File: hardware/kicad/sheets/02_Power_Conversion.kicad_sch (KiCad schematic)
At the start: 77 parts, among them U201 LMR38020F-Q1 adjustable-frequ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, U202 TPS2121RUXR priority power mux, U203 4.4..5.25 V synchronous buck 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, U204 SN74LVC1G08-Q1 — MAIN_INPUT_V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, U205 SN74LVC08A-Q1 quad AND — requ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, U206 TPS22918-Q1 OLED load switch, U207 TPS22918-Q1 SENSOR load switch, U208 TPS22918-Q1 UI load switch, U209 TPS2553-Q1 active-high EXPANS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, U210 TPS22918-Q1 RELAY logic branch, U211 TPS22918-Q1 FIELD-SENSE branch, U212 TPS2553-Q1 active-high motor-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, U213 TPS2553-Q1 active-high motor-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

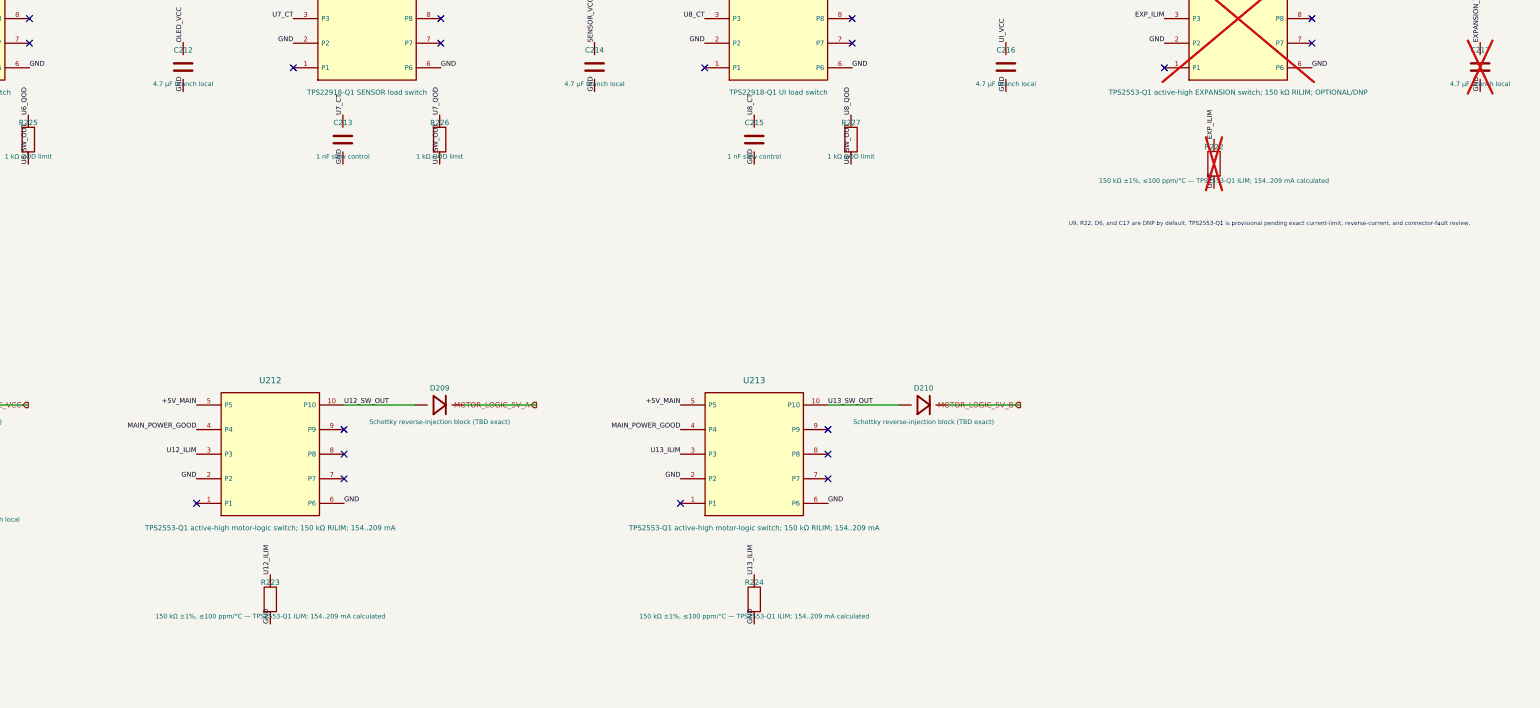
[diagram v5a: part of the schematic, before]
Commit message: Implement ECO-008R TPS2553 current limits
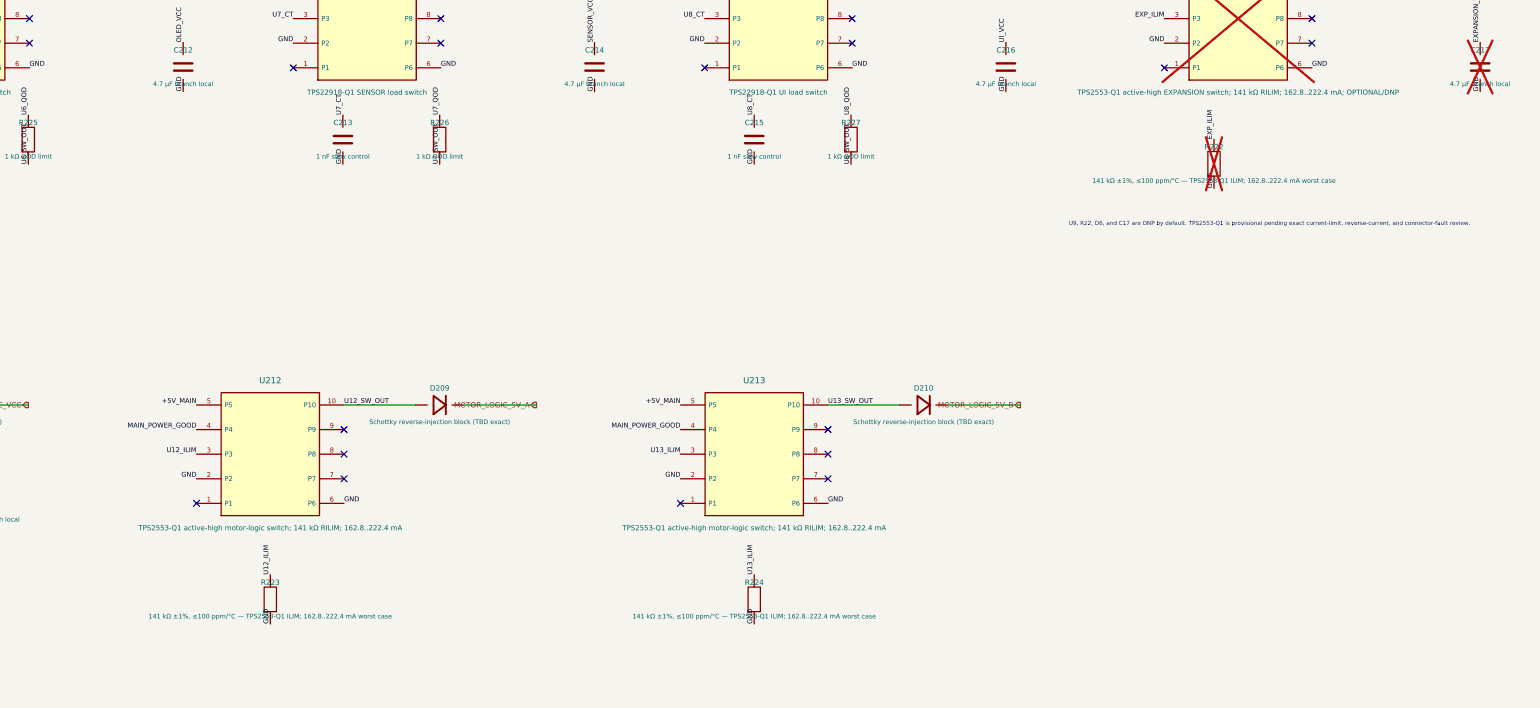
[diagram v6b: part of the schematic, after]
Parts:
- R222, R223, R224: value 150 kΩ ±1%, ≤100 ppm/°C — TPS2553-Q1 ILIM; 154..209 mA calculated -> 141 kΩ ±1%, ≤100 ppm/°C — TPS2553-Q1 ILIM; 162.8..222.4 mA worst case
- U209: value TPS2553-Q1 active-high EXPANSION switch; 150 kΩ RILIM; OPTIONAL/DNP -> TPS2553-Q1 active-high EXPANSION switch; 141 kΩ RILIM; 162.8..222.4 mA; OPTIONAL/DNP
- U212, U213: value TPS2553-Q1 active-high motor-logic switch; 150 kΩ RILIM; 154..209 mA -> TPS2553-Q1 active-high motor-logic switch; 141 kΩ RILIM; 162.8..222.4 mA
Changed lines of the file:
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@@
   (symbol (lib_id "IPC100:IC10") (at 455 155 0) (unit 1) (exclude_from_sim no) (in_bom yes) (on_board yes) (dnp yes)
     (property "Reference" "U209" (at 455 139.76 0) (effects (font (size 1.27 1.27))))
-    (property "Value" "TPS2553-Q1 active-high EXPANSION switch; 150 kΩ RILIM; OPTIONAL/DNP" (at 455 170.24 0) (effects (font (size 1.05 1.05))))
+    (property "Value" "TPS2553-Q1 active-high EXPANSION switch; 141 kΩ RILIM; 162.8..222.4 mA; OPTIONAL/DNP" (at 455 170.24 0) (effects (font (size 1.05 1.05))))
     (property "Footprint" "" (at 455 155 0) (effects (font (size 1 1)) hide))
     (property "Datasheet" "https://www.ti.com/lit/ds/symlink/tps2553-q1.pdf" (at 455 155 0) (effects (font (size 1 1)) hide))
@@
   (symbol (lib_id "IPC100:R") (at 450 185 90) (unit 1) (exclude_from_sim no) (in_bom yes) (on_board yes) (dnp yes)
     (property "Reference" "R222" (at 450 181.5 90) (effects (font (size 1.1 1.1))))
-    (property "Value" "150 kΩ ±1%, ≤100 ppm/°C — TPS2553-Q1 ILIM; 154..209 mA calculated" (at 450 188.5 90) (effects (font (size 0.95 0.95))))
+    (property "Value" "141 kΩ ±1%, ≤100 ppm/°C — TPS2553-Q1 ILIM; 162.8..222.4 mA worst case" (at 450 188.5 90) (effects (font (size 0.95 0.95))))
     (property "Footprint" "" (at 450 185 0) (effects (font (size 1 1)) hide))
     (property "Datasheet" "" (at 450 185 0) (effects (font (size 1 1)) hide))
@@
   (symbol (lib_id "IPC100:IC10") (at 255 245 0) (unit 1) (exclude_from_sim no) (in_bom yes) (on_board yes) (dnp no)
     (property "Reference" "U212" (at 255 229.76 0) (effects (font (size 1.27 1.27))))
-    (property "Value" "TPS2553-Q1 active-high motor-logic switch; 150 kΩ RILIM; 154..209 mA" (at 255 260.24 0) (effects (font (size 1.05 1.05))))
+    (property "Value" "TPS2553-Q1 active-high motor-logic switch; 141 kΩ RILIM; 162.8..222.4 mA" (at 255 260.24 0) (effects (font (size 1.05 1.05))))
     (property "Footprint" "" (at 255 245 0) (effects (font (size 1 1)) hide))
     (property "Datasheet" "https://www.ti.com/lit/ds/symlink/tps2553-q1.pdf" (at 255 245 0) (effects (font (size 1 1)) hide))
@@
   (symbol (lib_id "IPC100:R") (at 255 275 90) (unit 1) (exclude_from_sim no) (in_bom yes) (on_board yes) (dnp no)
     (property "Reference" "R223" (at 255 271.5 90) (effects (font (size 1.1 1.1))))
-    (property "Value" "150 kΩ ±1%, ≤100 ppm/°C — TPS2553-Q1 ILIM; 154..209 mA calculated" (at 255 278.5 90) (effects (font (size 0.95 0.95))))
+    (property "Value" "141 kΩ ±1%, ≤100 ppm/°C — TPS2553-Q1 ILIM; 162.8..222.4 mA worst case" (at 255 278.5 90) (effects (font (size 0.95 0.95))))
     (property "Footprint" "" (at 255 275 0) (effects (font (size 1 1)) hide))
     (property "Datasheet" "" (at 255 275 0) (effects (font (size 1 1)) hide))
@@
   (symbol (lib_id "IPC100:IC10") (at 355 245 0) (unit 1) (exclude_from_sim no) (in_bom yes) (on_board yes) (dnp no)
     (property "Reference" "U213" (at 355 229.76 0) (effects (font (size 1.27 1.27))))
-    (property "Value" "TPS2553-Q1 active-high motor-logic switch; 150 kΩ RILIM; 154..209 mA" (at 355 260.24 0) (effects (font (size 1.05 1.05))))
+    (property "Value" "TPS2553-Q1 active-high motor-logic switch; 141 kΩ RILIM; 162.8..222.4 mA" (at 355 260.24 0) (effects (font (size 1.05 1.05))))
     (property "Footprint" "" (at 355 245 0) (effects (font (size 1 1)) hide))
     (property "Datasheet" "https://www.ti.com/lit/ds/symlink/tps2553-q1.pdf" (at 355 245 0) (effects (font (size 1 1)) hide))
@@
   (symbol (lib_id "IPC100:R") (at 355 275 90) (unit 1) (exclude_from_sim no) (in_bom yes) (on_board yes) (dnp no)
     (property "Reference" "R224" (at 355 271.5 90) (effects (font (size 1.1 1.1))))
-    (property "Value" "150 kΩ ±1%, ≤100 ppm/°C — TPS2553-Q1 ILIM; 154..209 mA calculated" (at 355 278.5 90) (effects (font (size 0.95 0.95))))
+    (property "Value" "141 kΩ ±1%, ≤100 ppm/°C — TPS2553-Q1 ILIM; 162.8..222.4 mA worst case" (at 355 278.5 90) (effects (font (size 0.95 0.95))))
     (property "Footprint" "" (at 355 275 0) (effects (font (size 1 1)) hide))
     (property "Datasheet" "" (at 355 275 0) (effects (font (size 1 1)) hide))
